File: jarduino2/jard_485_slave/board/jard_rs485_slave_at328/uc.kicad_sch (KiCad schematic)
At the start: 12 parts, among them J7 ISCP, U5 ATmega328P-A, Y1 Resonator

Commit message: Nouvel essai de routage avec en + LEDs
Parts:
- removed TP20, TP21: TestPoint, TestPoint:TestPoint_Pad_D1.5mm, symbol Connector:TestPoint
- added D1: LED, LED_SMD:LED_0805_2012Metric_Pad1.15x1.40mm_HandSolder, symbol Device:LED
- added D3: LED, LED_THT:LED_D3.0mm_FlatTop, symbol Device:LED
- added R12: 220, Resistor_SMD:R_0805_2012Metric_Pad1.20x1.40mm_HandSolder, symbol Device:R
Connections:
- net GND: now also D1.1 (K), D3.1 (K)
- net at U5.12 (PB0): now also R12.1
- new net: D1.2 (A), D3.2 (A), R12.2
- no-connect marks 7 -> 6
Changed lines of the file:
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@@
   (junction (at 44.45 158.75) (diameter 0) (color 0 0 0 0)
   )
-  (junction (at 33.02 166.37) (diameter 0) (color 0 0 0 0)
+  (junction (at 179.07 95.25) (diameter 0) (color 0 0 0 0)
   )
   (junction (at 133.35 58.42) (diameter 0) (color 0 0 0 0)
@@
   (junction (at 133.35 83.82) (diameter 0) (color 0 0 0 0)
   )
-  (junction (at 195.58 133.35) (diameter 0) (color 0 0 0 0)
+  (junction (at 163.83 95.25) (diameter 0) (color 0 0 0 0)
   )
   (junction (at 187.96 133.35) (diameter 0) (color 0 0 0 0)
@@
   (no_connect (at 148.59 118.11))
   (no_connect (at 50.8 105.41))
-  (no_connect (at 148.59 95.25))
   (no_connect (at 148.59 151.13))
   (wire (pts (xy 148.59 107.95) (xy 151.13 107.95))
@@
     (stroke (width 0) (type default))
   )
+  (wire (pts (xy 163.83 95.25) (xy 166.37 95.25))
+    (stroke (width 0) (type default))
+  )
   (wire (pts (xy 162.56 106.68) (xy 170.18 106.68))
     (stroke (width 0) (type default))
@@
     (stroke (width 0) (type default))
   )
+  (wire (pts (xy 162.56 95.25) (xy 163.83 95.25))
+    (stroke (width 0) (type default))
+  )
   (wire (pts (xy 187.96 119.38) (xy 187.96 123.19))
     (stroke (width 0) (type default))
@@
     (stroke (width 0) (type default))
   )
+  (wire (pts (xy 173.99 85.09) (xy 179.07 85.09))
+    (stroke (width 0) (type default))
+  )
   (wire (pts (xy 187.96 133.35) (xy 187.96 130.81))
     (stroke (width 0) (type default))
@@
     (stroke (width 0) (type default))
   )
+  (wire (pts (xy 163.83 95.25) (xy 163.83 85.09))
+    (stroke (width 0) (type default))
+  )
+  (wire (pts (xy 179.07 95.25) (xy 179.07 96.52))
+    (stroke (width 0) (type default))
+  )
   (wire (pts (xy 133.35 46.99) (xy 133.35 58.42))
     (stroke (width 0) (type default))
@@
     (stroke (width 0) (type default))
   )
-  (wire (pts (xy 195.58 129.54) (xy 195.58 133.35))
+  (wire (pts (xy 173.99 95.25) (xy 179.07 95.25))
     (stroke (width 0) (type default))
   )
@@
     (stroke (width 0) (type default))
   )
-  (wire (pts (xy 29.21 166.37) (xy 33.02 166.37))
-    (stroke (width 0) (type default))
-  )
   (wire (pts (xy 151.13 58.42) (xy 151.13 69.85))
     (stroke (width 0) (type default))
@@
     (stroke (width 0) (type default))
   )
+  (wire (pts (xy 179.07 85.09) (xy 179.07 95.25))
+    (stroke (width 0) (type default))
+  )
   (wire (pts (xy 147.32 46.99) (xy 151.13 46.99))
     (stroke (width 0) (type default))
@@
     (stroke (width 0) (type default))
   )
-  (wire (pts (xy 33.02 166.37) (xy 46.99 166.37))
+  (wire (pts (xy 29.21 166.37) (xy 46.99 166.37))
     (stroke (width 0) (type default))
   )
@@
     (stroke (width 0) (type default))
   )
+  (wire (pts (xy 163.83 85.09) (xy 166.37 85.09))
+    (stroke (width 0) (type default))
+  )
   (wire (pts (xy 157.48 118.11) (xy 170.18 118.11))
     (stroke (width 0) (type default))
@@
     (stroke (width 0) (type default))
   )
-  (wire (pts (xy 195.58 133.35) (xy 187.96 133.35))
+  (wire (pts (xy 187.96 133.35) (xy 198.12 133.35))
     (stroke (width 0) (type default))
   )
@@
     (stroke (width 0) (type default))
   )
-  (wire (pts (xy 33.02 162.56) (xy 33.02 166.37))
-    (stroke (width 0) (type default))
-  )
   (wire (pts (xy 133.35 69.85) (xy 133.35 83.82))
     (stroke (width 0) (type default))
@@
     (stroke (width 0) (type default))
   )
-  (wire (pts (xy 195.58 133.35) (xy 198.12 133.35))
+  (wire (pts (xy 148.59 95.25) (xy 154.94 95.25))
     (stroke (width 0) (type default))
   )
@@
     )
   )
-  (symbol (lib_id "Connector:TestPoint") (at 195.58 129.54 0) (unit 1)
-    (in_bom yes) (on_board yes) (dnp no) (fields_autoplaced)
-    (property "Reference" "TP20" (at 196.977 125.214 0)
-      (effects (font (size 1.27 1.27)) (justify left))
-    )
-    (property "Value" "TestPoint" (at 196.977 127.262 0)
-      (effects (font (size 1.27 1.27)) (justify left))
-    )
-    (property "Footprint" "TestPoint:TestPoint_Pad_D1.5mm" (at 200.66 129.54 0)
-      (effects (font (size 1.27 1.27)) hide)
-    )
-    (property "Datasheet" "~" (at 200.66 129.54 0)
-      (effects (font (size 1.27 1.27)) hide)
-    )
-    (pin "1")
-    (instances
-      (project "jard_rs485_slave_at328"
-        (path "/5ae93d62-0543-4c0e-b37d-d67af6219e1b/36e9fbeb-2032-4e73-95af-53e316cf916d"
-          (reference "TP20") (unit 1)
-        )
-      )
-    )
-  )
   (symbol (lib_id "power:GND") (at 60.96 158.75 90) (unit 1)
     (in_bom yes) (on_board yes) (dnp no) (fields_autoplaced)
@@
     )
   )
+  (symbol (lib_id "power:GND") (at 179.07 96.52 0) (unit 1)
+    (in_bom yes) (on_board yes) (dnp no) (fields_autoplaced)
+    (property "Reference" "#PWR07" (at 179.07 102.87 0)
+      (effects (font (size 1.27 1.27)) hide)
+    )
+    (property "Value" "GND" (at 179.07 100.465 0)
+      (effects (font (size 1.27 1.27)))
+    )
+    (property "Footprint" "" (at 179.07 96.52 0)
+      (effects (font (size 1.27 1.27)) hide)
+    )
+    (property "Datasheet" "" (at 179.07 96.52 0)
+      (effects (font (size 1.27 1.27)) hide)
+    )
+    (pin "1")
+    (instances
+      (project "jard_rs485_slave_at328"
+        (path "/5ae93d62-0543-4c0e-b37d-d67af6219e1b/36e9fbeb-2032-4e73-95af-53e316cf916d"
+          (reference "#PWR07") (unit 1)
+        )
+      )
+    )
+  )
   (symbol (lib_id "power:GND") (at 101.6 95.25 270) (unit 1)
     (in_bom yes) (on_board yes) (dnp no) (fields_autoplaced)
@@
     )
   )
+  (symbol (lib_id "Device:LED") (at 170.18 95.25 180) (unit 1)
+    (in_bom yes) (on_board yes) (dnp no) (fields_autoplaced)
+    (property "Reference" "D1" (at 171.7675 89.511 0)
+      (effects (font (size 1.27 1.27)))
+    )
+    (property "Value" "LED" (at 171.7675 91.559 0)
+      (effects (font (size 1.27 1.27)))
+    )
+    (property "Footprint" "LED_SMD:LED_0805_2012Metric_Pad1.15x1.40mm_HandSolder" (at 170.18 95.25 0)
+      (effects (font (size 1.27 1.27)) hide)
+    )
+    (property "Datasheet" "~" (at 170.18 95.25 0)
+      (effects (font (size 1.27 1.27)) hide)
+    )
+    (pin "1")
+    (pin "2")
+    (instances
+      (project "jard_rs485_slave_at328"
+        (path "/5ae93d62-0543-4c0e-b37d-d67af6219e1b/36e9fbeb-2032-4e73-95af-53e316cf916d"
+          (reference "D1") (unit 1)
+        )
+      )
+    )
+  )
   (symbol (lib_id "power:+5V") (at 133.35 45.72 0) (unit 1)
     (in_bom yes) (on_board yes) (dnp no) (fields_autoplaced)
@@
         (path "/5ae93d62-0543-4c0e-b37d-d67af6219e1b/36e9fbeb-2032-4e73-95af-53e316cf916d"
           (reference "Y1") (unit 1)
-        )
-      )
-    )
-  )
-  (symbol (lib_id "Connector:TestPoint") (at 33.02 162.56 0) (unit 1)
-    (in_bom yes) (on_board yes) (dnp no) (fields_autoplaced)
-    (property "Reference" "TP21" (at 34.417 158.234 0)
-      (effects (font (size 1.27 1.27)) (justify left))
-    )
-    (property "Value" "TestPoint" (at 34.417 160.282 0)
-      (effects (font (size 1.27 1.27)) (justify left))
-    )
-    (property "Footprint" "TestPoint:TestPoint_Pad_D1.5mm" (at 38.1 162.56 0)
-      (effects (font (size 1.27 1.27)) hide)
-    )
-    (property "Datasheet" "~" (at 38.1 162.56 0)
-      (effects (font (size 1.27 1.27)) hide)
-    )
-    (pin "1")
-    (instances
-      (project "jard_rs485_slave_at328"
-        (path "/5ae93d62-0543-4c0e-b37d-d67af6219e1b/36e9fbeb-2032-4e73-95af-53e316cf916d"
-          (reference "TP21") (unit 1)
         )
       )
@@
     )
   )
+  (symbol (lib_id "Device:R") (at 158.75 95.25 90) (unit 1)
+    (in_bom yes) (on_board yes) (dnp no) (fields_autoplaced)
+    (property "Reference" "R12" (at 158.75 90.654 90)
+      (effects (font (size 1.27 1.27)))
+    )
+    (property "Value" "220" (at 158.75 92.702 90)
+      (effects (font (size 1.27 1.27)))
+    )
+    (property "Footprint" "Resistor_SMD:R_0805_2012Metric_Pad1.20x1.40mm_HandSolder" (at 158.75 97.028 90)
+      (effects (font (size 1.27 1.27)) hide)
+    )
+    (property "Datasheet" "~" (at 158.75 95.25 0)
+      (effects (font (size 1.27 1.27)) hide)
+    )
+    (pin "1")
+    (pin "2")
+    (instances
+      (project "jard_rs485_slave_at328"
+        (path "/5ae93d62-0543-4c0e-b37d-d67af6219e1b/36e9fbeb-2032-4e73-95af-53e316cf916d"
+          (reference "R12") (unit 1)
+        )
+      )
+    )
+  )
   (symbol (lib_id "Device:C") (at 143.51 69.85 270) (unit 1)
     (in_bom yes) (on_board yes) (dnp no) (fields_autoplaced)
@@
         )
       )
+    )
+  )
+  (symbol (lib_id "Device:LED") (at 170.18 85.09 180) (unit 1)
+    (in_bom yes) (on_board yes) (dnp no) (fields_autoplaced)
+    (property "Reference" "D3" (at 171.7675 79.351 0)
+      (effects (font (size 1.27 1.27)))
+    )
+    (property "Value" "LED" (at 171.7675 81.399 0)
+      (effects (font (size 1.27 1.27)))
+    )
+    (property "Footprint" "LED_THT:LED_D3.0mm_FlatTop" (at 170.18 85.09 0)
+      (effects (font (size 1.27 1.27)) hide)
+    )
+    (property "Datasheet" "~" (at 170.18 85.09 0)
+      (effects (font (size 1.27 1.27)) hide)
+    )
+    (pin "1")
+    (pin "2")
+    (instances
+      (project "jard_rs485_slave_at328"
+        (path "/5ae93d62-0543-4c0e-b37d-d67af6219e1b/36e9fbeb-2032-4e73-95af-53e316cf916d"
+          (reference "D3") (unit 1)
+        )
+      )

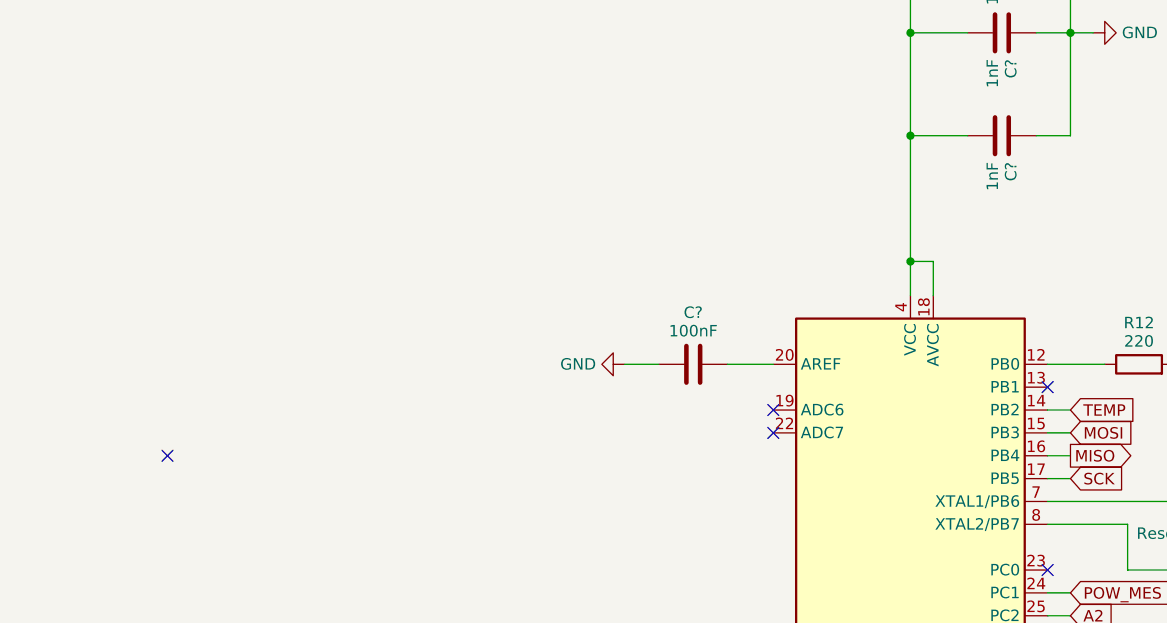
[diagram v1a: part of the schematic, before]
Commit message: Re-routage en gagnant de la place (à finir)
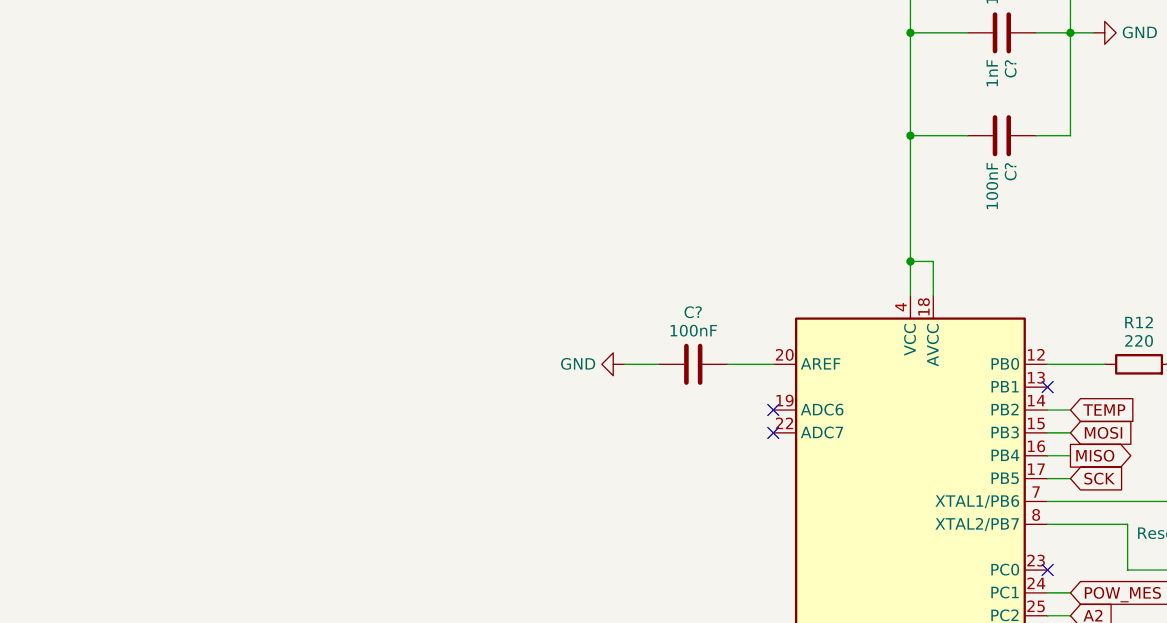
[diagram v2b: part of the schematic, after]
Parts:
- removed C?: 1nF, Capacitor_SMD:C_0603_1608Metric, symbol Device:C
- removed C?: 100nF, Capacitor_SMD:C_0603_1608Metric, symbol Device:C
- added C? (x2): 100nF, Capacitor_SMD:C_0603_1608Metric, symbol Device:C
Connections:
- net +5V: now also C?.2, C?.2
- net GND: now also C?.1, C?.1
- no-connect marks 6 -> 5
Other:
- company: (none) -> BPC
- title: (none) -> Carte de commande d'un Oya par RS485
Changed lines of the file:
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@@
 (kicad_sch (version 20230121) (generator eeschema)
   (paper "A4")
+  (title_block
+    (title "Carte de commande d'un Oya par RS485")
+    (date "2024-03-29")
+    (rev "D0")
+    (company "BPC")
+    (comment 1 "Technologie CMD basée sur ATMEGA328")
+    (comment 2 "Monitoring de tension d'alimentation")
+    (comment 3 "1 sortie 12V/5A - 2 entrées TOR - 1 débimètre - 1 LED - Temp -RS485")
+  )
   (junction (at 133.35 46.99) (diameter 0) (color 0 0 0 0)
   )
@@
   (no_connect (at 118.11 100.33))
   (no_connect (at 148.59 118.11))
-  (no_connect (at 50.8 105.41))
   (no_connect (at 148.59 151.13))
   (wire (pts (xy 148.59 107.95) (xy 151.13 107.95))
@@
         (path "/5ae93d62-0543-4c0e-b37d-d67af6219e1b/36e9fbeb-2032-4e73-95af-53e316cf916d"
           (reference "#PWR030") (unit 1)
+        )
+      )
+    )
+  )
+  (symbol (lib_id "Device:C") (at 143.51 69.85 270) (unit 1)
+    (in_bom yes) (on_board yes) (dnp no) (fields_autoplaced)
+    (property "Reference" "C?" (at 144.534 72.771 0)
+      (effects (font (size 1.27 1.27)) (justify left))
+    )
+    (property "Value" "100nF" (at 142.486 72.771 0)
+      (effects (font (size 1.27 1.27)) (justify left))
+    )
+    (property "Footprint" "Capacitor_SMD:C_0603_1608Metric" (at 139.7 70.8152 0)
+      (effects (font (size 1.27 1.27)) hide)
+    )
+    (property "Datasheet" "~" (at 143.51 69.85 0)
+      (effects (font (size 1.27 1.27)) hide)
+    )
+    (pin "1")
+    (pin "2")
+    (instances
+      (project "jard_rs485_slave_at328"
+        (path "/5ae93d62-0543-4c0e-b37d-d67af6219e1b"
+          (reference "C?") (unit 1)
+        )
+        (path "/5ae93d62-0543-4c0e-b37d-d67af6219e1b/dd36e5af-5314-42bf-9b88-ba8e41ec06f7"
+          (reference "C?") (unit 1)
+        )
+        (path "/5ae93d62-0543-4c0e-b37d-d67af6219e1b/36e9fbeb-2032-4e73-95af-53e316cf916d"
+          (reference "C9") (unit 1)
         )
       )
@@
     )
   )
-  (symbol (lib_id "Device:R") (at 158.75 95.25 90) (unit 1)
-    (in_bom yes) (on_board yes) (dnp no) (fields_autoplaced)
-    (property "Reference" "R12" (at 158.75 90.654 90)
-      (effects (font (size 1.27 1.27)))
-    )
-    (property "Value" "220" (at 158.75 92.702 90)
-      (effects (font (size 1.27 1.27)))
-    )
-    (property "Footprint" "Resistor_SMD:R_0805_2012Metric_Pad1.20x1.40mm_HandSolder" (at 158.75 97.028 90)
-      (effects (font (size 1.27 1.27)) hide)
-    )
-    (property "Datasheet" "~" (at 158.75 95.25 0)
-      (effects (font (size 1.27 1.27)) hide)
-    )
-    (pin "1")
-    (pin "2")
-    (instances
-      (project "jard_rs485_slave_at328"
-        (path "/5ae93d62-0543-4c0e-b37d-d67af6219e1b/36e9fbeb-2032-4e73-95af-53e316cf916d"
-          (reference "R12") (unit 1)
-        )
-      )
-    )
-  )
-  (symbol (lib_id "Device:C") (at 143.51 69.85 270) (unit 1)
-    (in_bom yes) (on_board yes) (dnp no) (fields_autoplaced)
-    (property "Reference" "C?" (at 144.534 72.771 0)
-      (effects (font (size 1.27 1.27)) (justify left))
-    )
-    (property "Value" "1nF" (at 142.486 72.771 0)
-      (effects (font (size 1.27 1.27)) (justify left))
-    )
-    (property "Footprint" "Capacitor_SMD:C_0603_1608Metric" (at 139.7 70.8152 0)
-      (effects (font (size 1.27 1.27)) hide)
-    )
-    (property "Datasheet" "~" (at 143.51 69.85 0)
+  (symbol (lib_id "Device:C") (at 143.51 46.99 270) (unit 1)
+    (in_bom yes) (on_board yes) (dnp no) (fields_autoplaced)
+    (property "Reference" "C?" (at 144.534 49.911 0)
+      (effects (font (size 1.27 1.27)) (justify left))
+    )
+    (property "Value" "100nF" (at 142.486 49.911 0)
+      (effects (font (size 1.27 1.27)) (justify left))
+    )
+    (property "Footprint" "Capacitor_SMD:C_0603_1608Metric" (at 139.7 47.9552 0)
+      (effects (font (size 1.27 1.27)) hide)
+    )
+    (property "Datasheet" "~" (at 143.51 46.99 0)
       (effects (font (size 1.27 1.27)) hide)
     )
@@
     )
   )
+  (symbol (lib_id "Device:R") (at 158.75 95.25 90) (unit 1)
+    (in_bom yes) (on_board yes) (dnp no) (fields_autoplaced)
+    (property "Reference" "R12" (at 158.75 90.654 90)
+      (effects (font (size 1.27 1.27)))
+    )
+    (property "Value" "220" (at 158.75 92.702 90)
+      (effects (font (size 1.27 1.27)))
+    )
+    (property "Footprint" "Resistor_SMD:R_0805_2012Metric_Pad1.20x1.40mm_HandSolder" (at 158.75 97.028 90)
+      (effects (font (size 1.27 1.27)) hide)
+    )
+    (property "Datasheet" "~" (at 158.75 95.25 0)
+      (effects (font (size 1.27 1.27)) hide)
+    )
+    (pin "1")
+    (pin "2")
+    (instances
+      (project "jard_rs485_slave_at328"
+        (path "/5ae93d62-0543-4c0e-b37d-d67af6219e1b/36e9fbeb-2032-4e73-95af-53e316cf916d"
+          (reference "R12") (unit 1)
+        )
+      )
+    )
+  )
   (symbol (lib_id "power:+5V") (at 241.3 58.42 0) (unit 1)
     (in_bom yes) (on_board yes) (dnp no) (fields_autoplaced)
@@
         )
       )
-    )
-  )
-  (symbol (lib_id "Device:C") (at 143.51 46.99 270) (unit 1)
-    (in_bom yes) (on_board yes) (dnp no) (fields_autoplaced)
-    (property "Reference" "C?" (at 144.534 49.911 0)
-      (effects (font (size 1.27 1.27)) (justify left))
-    )
-    (property "Value" "100nF" (at 142.486 49.911 0)
-      (effects (font (size 1.27 1.27)) (justify left))
-    )
-    (property "Footprint" "Capacitor_SMD:C_0603_1608Metric" (at 139.7 47.9552 0)
-      (effects (font (size 1.27 1.27)) hide)
-    )
-    (property "Datasheet" "~" (at 143.51 46.99 0)
-      (effects (font (size 1.27 1.27)) hide)
-    )
-    (pin "1")
-    (pin "2")
-    (instances
-      (project "jard_rs485_slave_at328"
-        (path "/5ae93d62-0543-4c0e-b37d-d67af6219e1b"
-          (reference "C?") (unit 1)
-        )
-        (path "/5ae93d62-0543-4c0e-b37d-d67af6219e1b/dd36e5af-5314-42bf-9b88-ba8e41ec06f7"
-          (reference "C?") (unit 1)
-        )
-        (path "/5ae93d62-0543-4c0e-b37d-d67af6219e1b/36e9fbeb-2032-4e73-95af-53e316cf916d"
-          (reference "C9") (unit 1)
-        )
-      )

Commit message: Petites coquilles de dossier
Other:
- title: Carte de commande d'un Oya par RS485 -> Carte de commande d'un OYA par RS485
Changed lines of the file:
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@@
   (paper "A4")
   (title_block
-    (title "Carte de commande d'un Oya par RS485")
+    (title "Carte de commande d'un OYA par RS485")
     (date "2024-03-29")
     (rev "D0")
     (company "BPC")
-    (comment 1 "Technologie CMD basée sur ATMEGA328")
+    (comment 1 "Technologie CMS basée sur ATMEGA328")
     (comment 2 "Monitoring de tension d'alimentation")
-    (comment 3 "1 sortie 12V/5A - 2 entrées TOR - 1 débimètre - 1 LED - Temp -RS485")
+    (comment 3 "1 sortie 12V/5A - 2 entrées TOR - 1 débimètre - 1 LED - Temp - RS485")
   )
   (junction (at 133.35 46.99) (diameter 0) (color 0 0 0 0)

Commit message: Suite revue: - Retrait limiteur de courant NOK pour flowmeter - Résolution des erreurs PCB
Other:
- title: Carte de commande d'un OYA par RS485 -> Carte de commande d'un OYA - Esclave RS485
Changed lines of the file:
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@@
   (paper "A4")
   (title_block
-    (title "Carte de commande d'un OYA par RS485")
-    (date "2024-03-29")
+    (title "Carte de commande d'un OYA - Esclave RS485")
+    (date "2024-03-31")
     (rev "D0")
     (company "BPC")
